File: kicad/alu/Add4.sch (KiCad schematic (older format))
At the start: 17 parts, among them U100 SN74ALVC00, U101 SN74ALVC00, U102 SN74ALVC00, U103 SN74ALVC00, U104 SN74ALVC00, U105 SN74ALVC00, U106 SN74ALVC00, U107 SN74ALVC00, U108 SN74ALVC00, U109 SN74ALVC00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

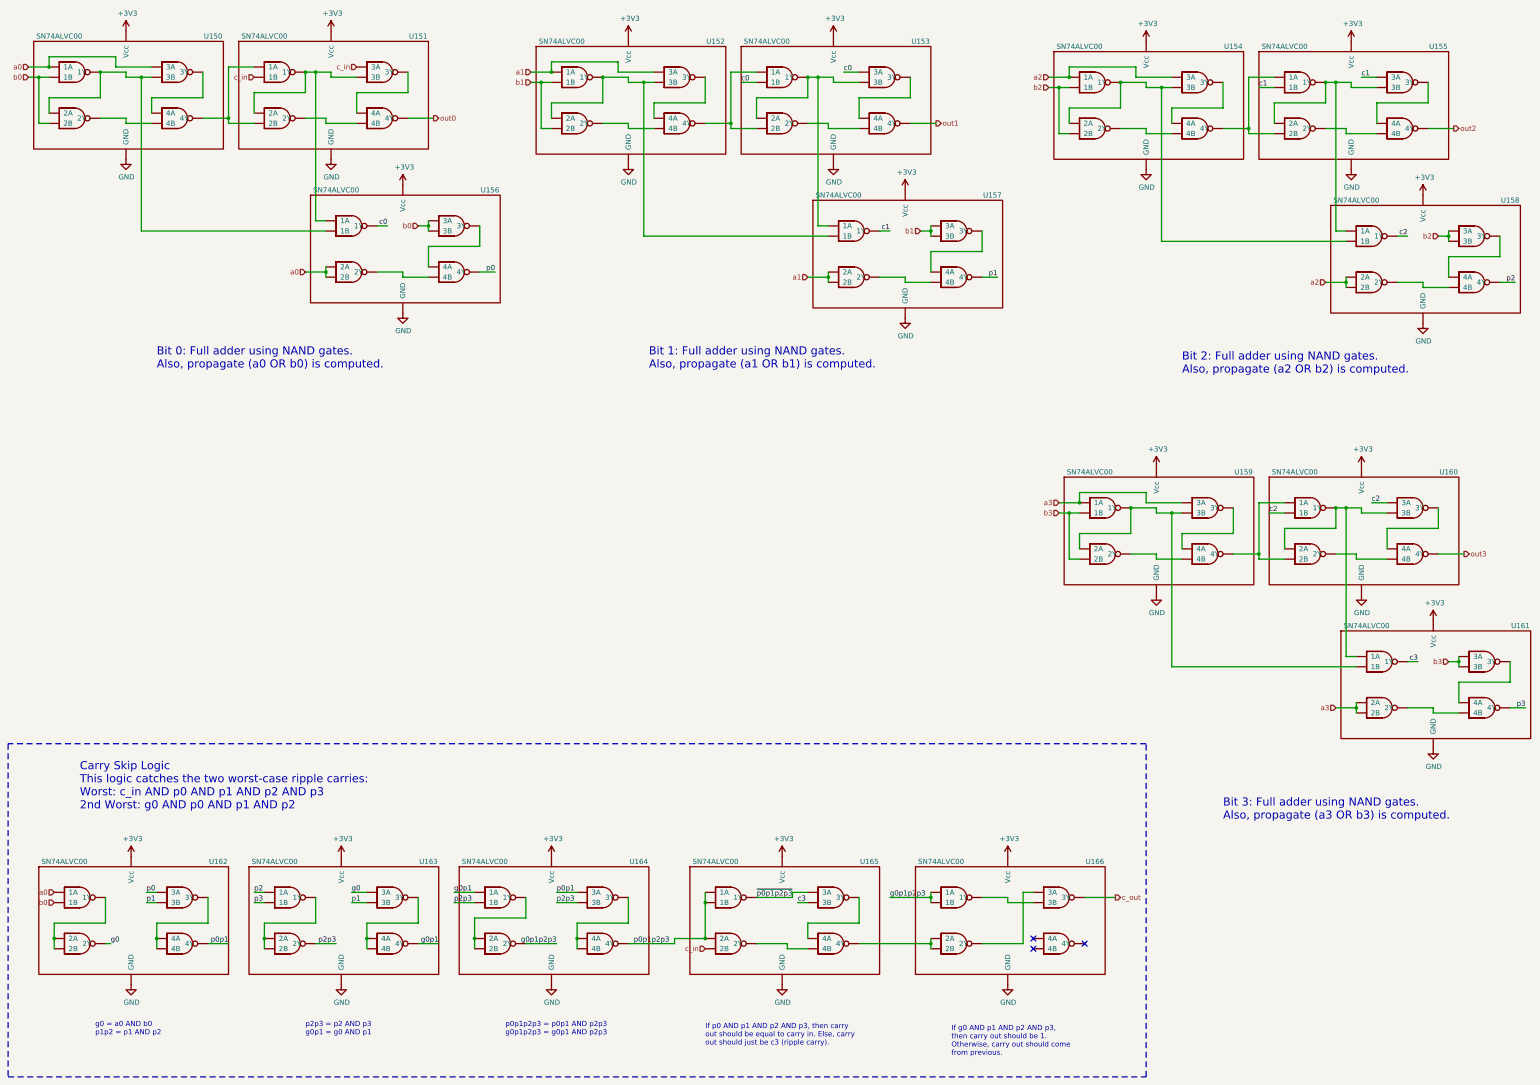
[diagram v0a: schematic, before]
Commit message: ALU schematic, layout, routing complete. Associated motherboardmod. Also added Load LED to register and program counter boards.
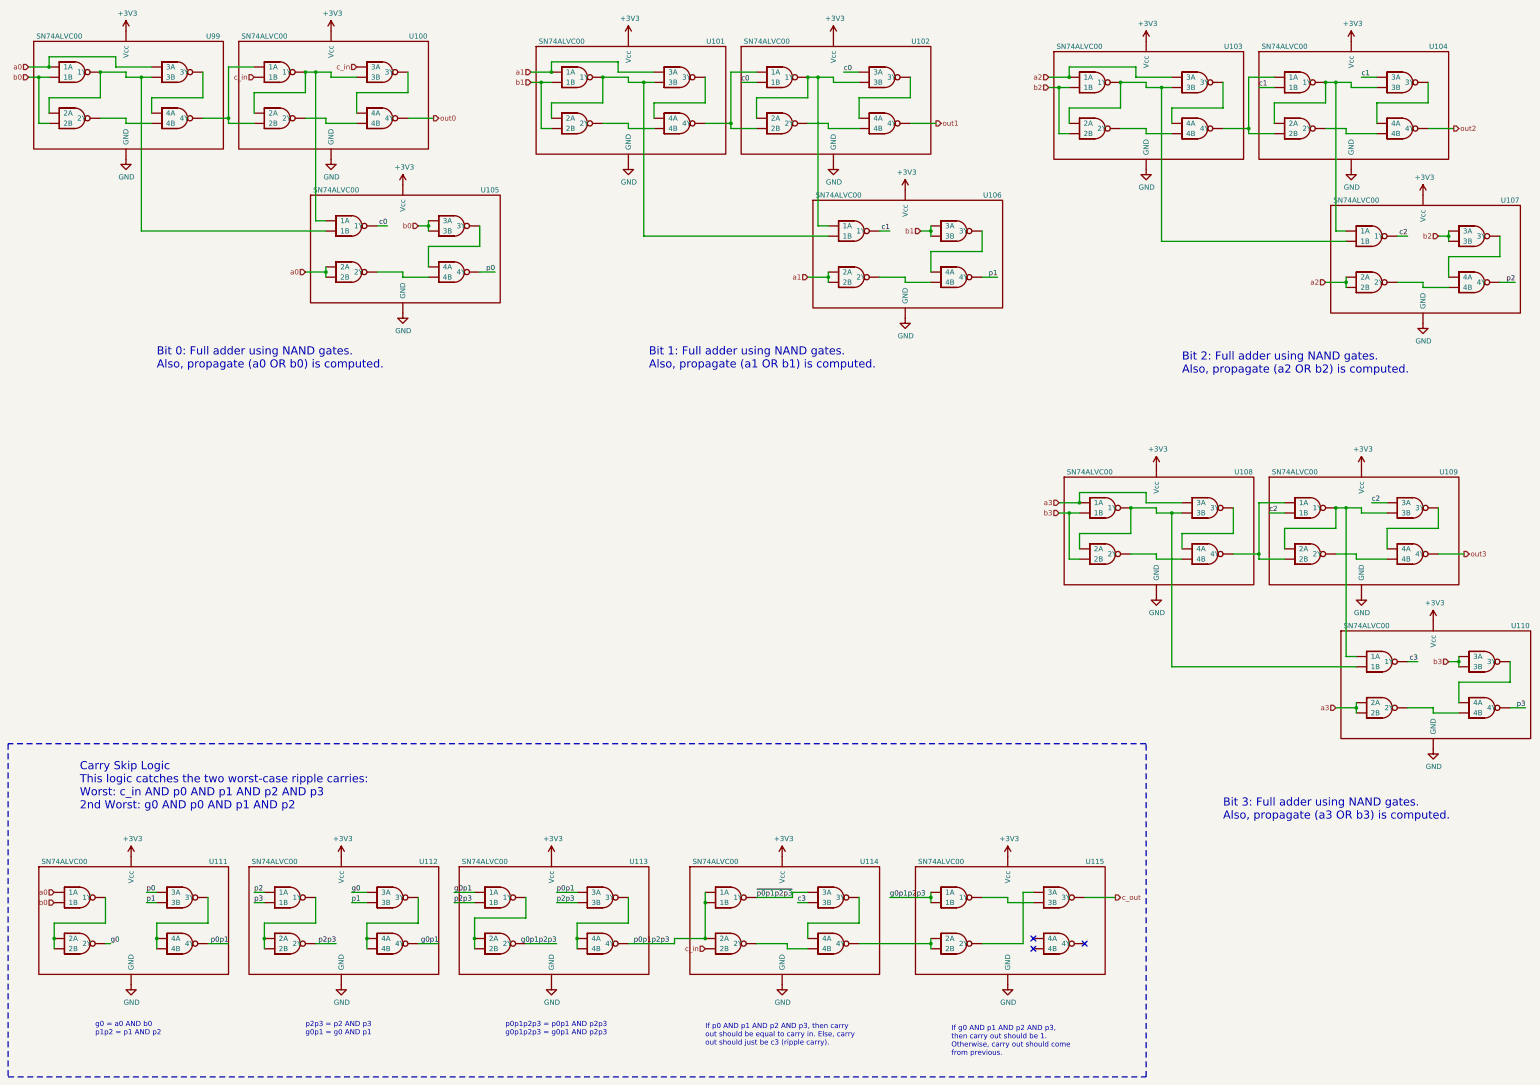
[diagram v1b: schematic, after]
